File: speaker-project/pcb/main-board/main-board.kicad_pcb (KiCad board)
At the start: 2 copper layers, 100 x 80 mm, 173 parts, among them J1 XT30U-M, J10 UART0, J11 USB-C, J12 JTAG, J13 BT-Modul, J14 Button-PCB, J2 JST-XH-5, J3 JST-XH-5, J4 CHG-STAT, J5 ICP5/USBi, J6 AuxIn 3.5mm, J7 FR-L, J8 FR-R, J9 SUB, Q1 AO4407A, Q2 AO4407A, Q3 MMBT3904, Q4 BC807-40, SW1 RESET, SW2 BOOT, U1 LMR33630ADDA, U2 AMS1117-3.3, U3 ADAU1701JSTZ, U4 24LC32A, U6 TPA3118D2DAP, U7 TPA3118D2DAP, U8 ESP32-S3-WROOM-1-N8R2, U9 USBLC6-2SC6, Y1 12.288MHz

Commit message: PCB-Fix: alle Stecker-Pads innerhalb der Platinenkante
- J1 (XT30) lag mit Pin 2 auf y=0, J4 (CHG-Header) mit Pins bei x>100,
  J13 (BT-Header) ragte senkrecht ueber die Unterkante hinaus
- J1 auf rot0 (58,5), J4 vertikal an (97,14), J13 war bereits gedreht
- Automatische Kantenpruefung ergaenzt: kein Pad ausserhalb 0..100/0..80
  (Ausnahmen: USB-C-Buchse und ESP32-Antenne, beabsichtigter Ueberhang)
- Fertigungsdaten (Gerber/Drill/Pos/BOM/SVG) neu exportiert

Co-Authored-By: Claude Fable 5 <noreply@anthropic.com>
Claude-Session: https://claude.ai/code/session_01L8xsupY9ovG6C5NDPPgqaH
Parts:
- moved C11 88.6 mm to (94.5, 22.5)
- moved C49 74.9 mm to (3.80, 48.6)
- moved C52 66.9 mm to (12.3, 52.6)
- moved C6 66.9 mm to (36.8, 62.6)
- moved C51 66.7 mm to (8.30, 51.6)
- moved C66 65.6 mm to (77.8, 55.6)
- moved C5 55.5 mm to (44.8, 60.6)
- moved C28 50.7 mm to (87.5, 30.5)
- moved C29 50.4 mm to (91.0, 30.5)
- moved R8 49.7 mm to (65.8, 56.6)
- moved C71 46.0 mm to (82.0, 55.8)
- moved R60 45.7 mm to (36.8, 60.1)
- moved C10 43.2 mm to (69.0, 34.8)
- moved D6 42.0 mm to (61.8, 56.6)
- moved R12 41.6 mm to (91.0, 27.4)
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
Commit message: Gehaeuse v2 'Boombox' (Motion-Boom-Stil) + Button-Board vollstaendig geroutet
Gehaeuse: Trapez-Buegelgriff, R22-Kanten + 45-Grad-Fasen, versenkte
Bedienmulde, vollflaechiger Hex-Grill (Press-Fit), Verstrebungsrippen,
Silikonfuss-Kanaele; 3 stuetzenfreie STLs, wasserdicht verifiziert,
Luftdichtheit der Kammern per Ray-Casting geprueft.

PCB: eigener Grid-A*-Autorouter (scipy-Dilationsmasken, Rip-up-Runden,
Seed-Randomisierung, GND-Stitching + SMD-GND-Anbindung, Via-Dedupe).
Button-Board: 100% geroutet, 0 Clearance-/Courtyard-Fehler; einzige
Restmeldung ist ein bekannter KiCad-7-Zonen-Falschalarm (GND-Kontinuitaet
per Polygon-Analyse nachgewiesen). USB-C-Ausrichtung am Main-Board gefixt.

Co-Authored-By: Claude Fable 5 <noreply@anthropic.com>
Claude-Session: https://claude.ai/code/session_01L8xsupY9ovG6C5NDPPgqaH
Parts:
- turned J11 to 90 degrees

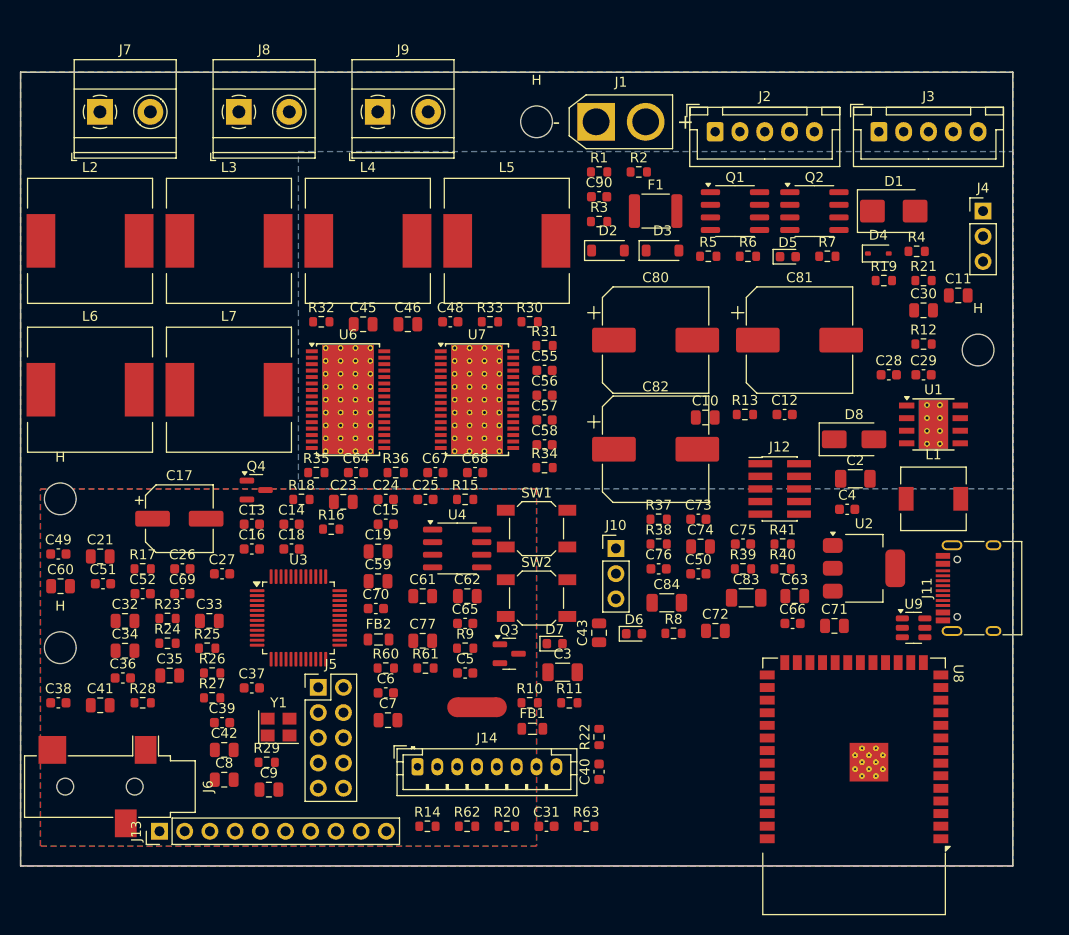
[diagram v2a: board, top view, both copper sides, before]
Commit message: WIP Routing-Vorbereitung: routbare Packabstaende (gap 0.8), Cache-Packung ohne SWIG-Leichen, Router longest-first + Budget-Tuning, FB1 fixiert
Main-Board-Layout hier noch ungeroutet — das geroutete Board folgt nach
Abschluss des laufenden Seed-Sweeps mit DRC-Ergebnis.

Co-Authored-By: Claude Fable 5 <noreply@anthropic.com>
Claude-Session: https://claude.ai/code/session_01L8xsupY9ovG6C5NDPPgqaH
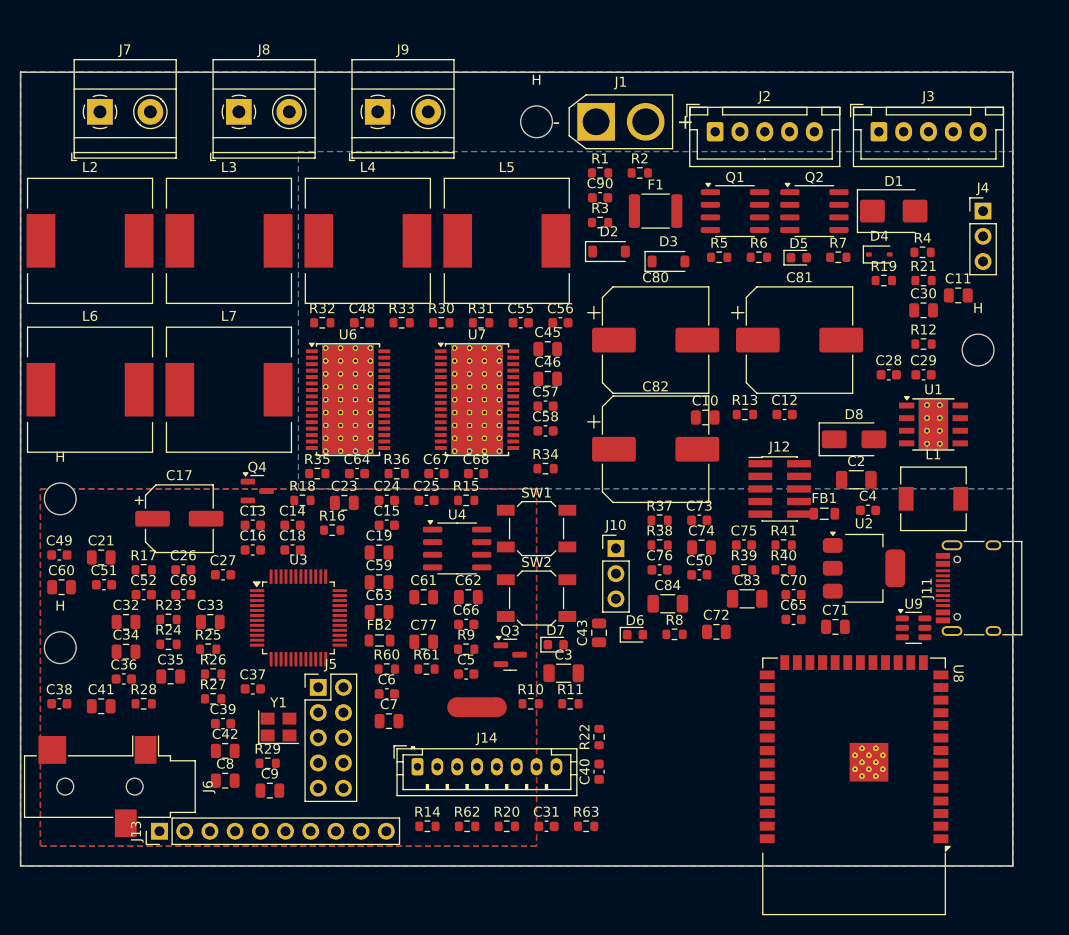
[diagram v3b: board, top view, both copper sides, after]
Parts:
- moved C70 42.1 mm to (77.9, 52.7)
- moved C63 41.9 mm to (36.1, 54.4)
- moved FB1 36.5 mm to (81.0, 44.5)
- moved C65 33.1 mm to (77.9, 55.2)
- moved C66 32.9 mm to (44.9, 55.7)
- moved C45 18.8 mm to (53.1, 27.9)
- moved C46 15.1 mm to (53.1, 30.9)
- moved C48 8.90 mm to (34.4, 25.3)
- moved R30 8.90 mm to (42.4, 25.3)
- moved R33 8.90 mm to (38.4, 25.3)
- moved C56 7.47 mm to (54.4, 25.3)
- moved R31 6.80 mm to (46.4, 25.3)
- moved C55 5.37 mm to (50.4, 25.3)
- moved C4 2.10 mm to (85.4, 44.2)
- moved C57 1.40 mm to (52.9, 33.7)
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
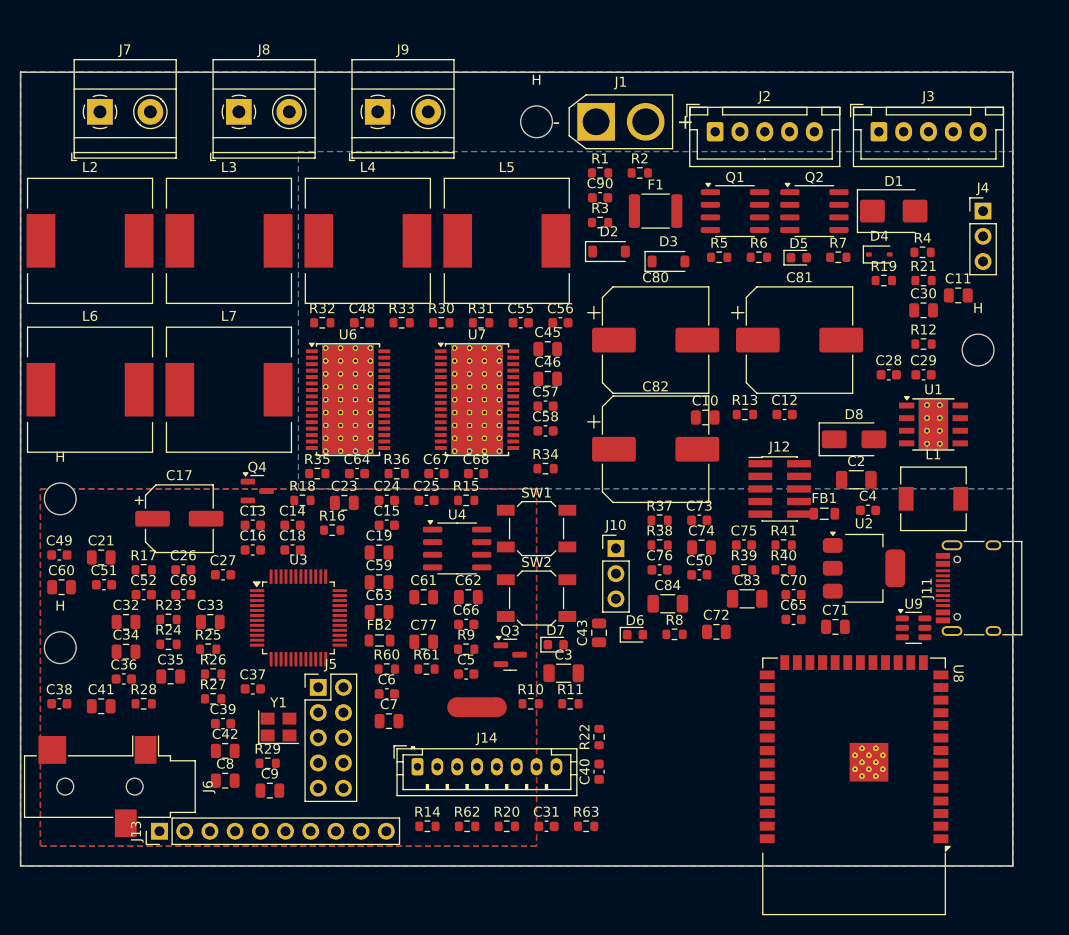
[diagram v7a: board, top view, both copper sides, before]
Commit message: WIP: Packabstand 1.1mm (Via-Plaetze), Buck-Bauteile fixiert, Rip-up abschaltbar
Co-Authored-By: Claude Fable 5 <noreply@anthropic.com>
Claude-Session: https://claude.ai/code/session_01L8xsupY9ovG6C5NDPPgqaH
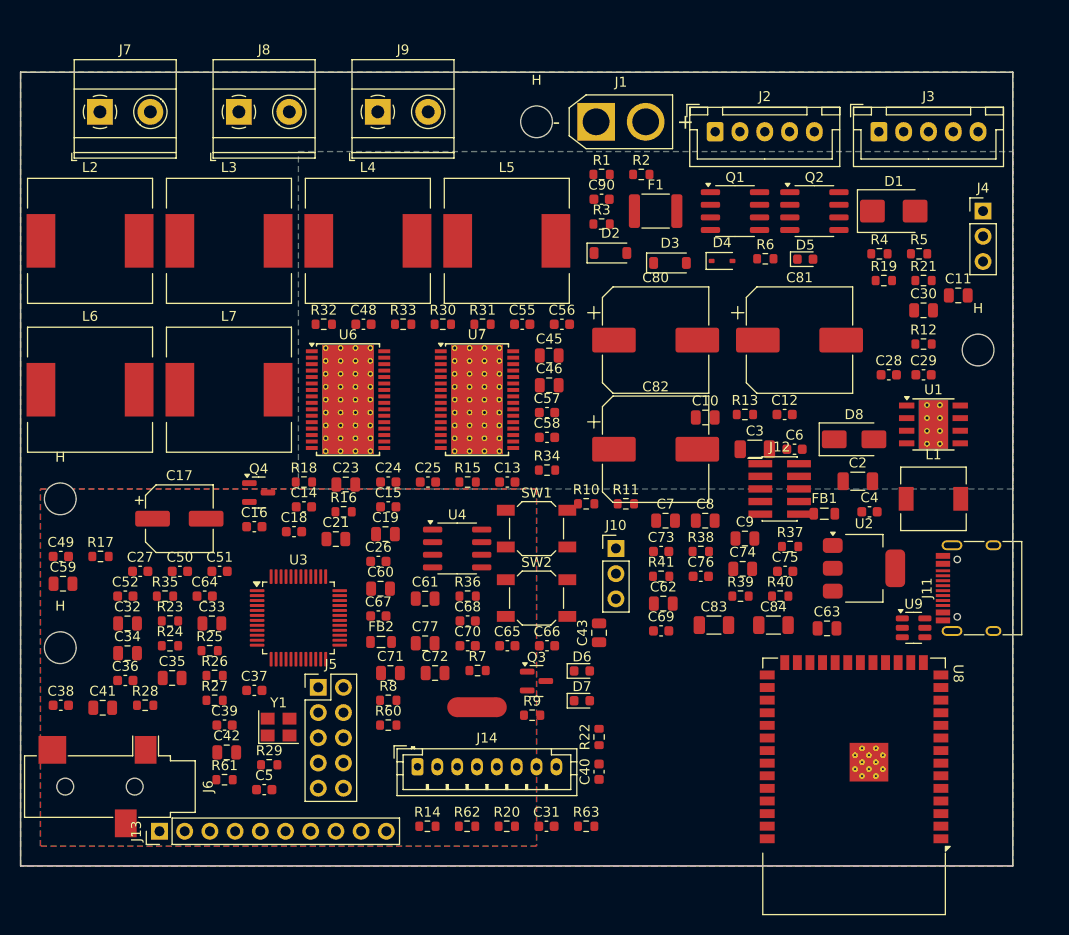
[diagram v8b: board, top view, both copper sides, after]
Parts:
- moved R7 55.3 mm to (46.1, 60.3)
- moved C8 55.0 mm to (69.0, 45.2)
- moved C9 54.2 mm to (73.0, 47.0)
- moved C50 52.4 mm to (16.1, 50.3)
- moved C69 48.3 mm to (64.6, 56.3)
- moved C6 47.9 mm to (78.0, 38.0)
- moved C63 45.2 mm to (81.3, 56.1)
- moved C71 45.1 mm to (37.3, 60.6)
- moved C7 34.4 mm to (65.0, 45.2)
- moved C70 33.3 mm to (45.1, 57.8)
- moved C60 32.2 mm to (36.3, 52.1)
- moved C59 31.9 mm to (4.28, 51.6)
- moved C3 29.7 mm to (74.0, 38.0)
- moved R8 29.6 mm to (37.1, 63.3)
- moved C65 29.0 mm to (49.1, 57.8)
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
